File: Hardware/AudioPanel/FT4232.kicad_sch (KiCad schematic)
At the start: 37 parts, among them U30 93LCxxA, U57 AP2112K-3.3, U59 FT4232H, Y5 12MHz

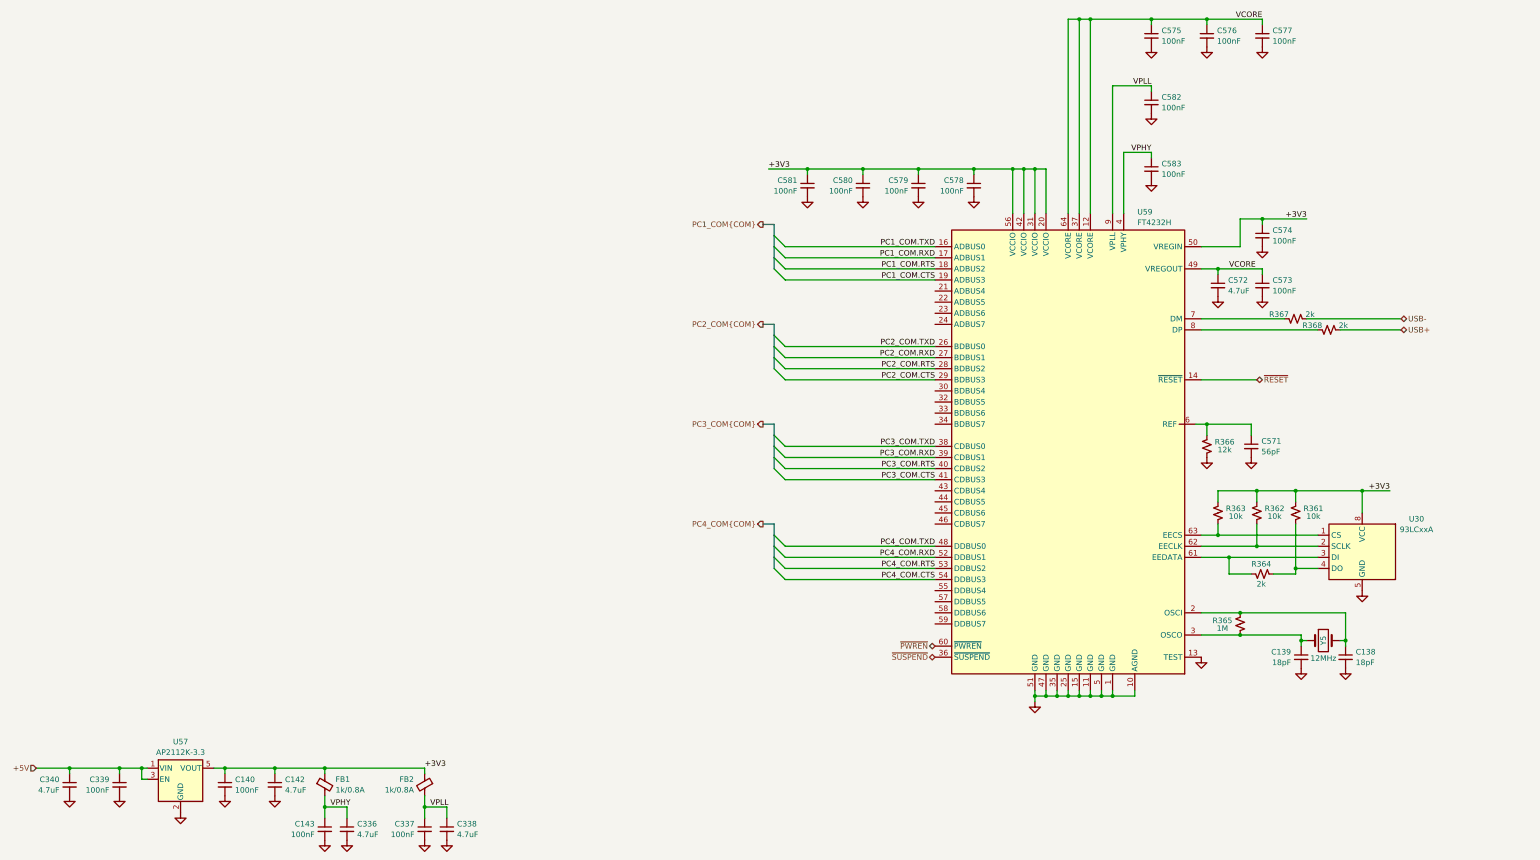
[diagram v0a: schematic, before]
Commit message: Realized that I need to rethink how I'm going to mix the radio audio with the stereo audio
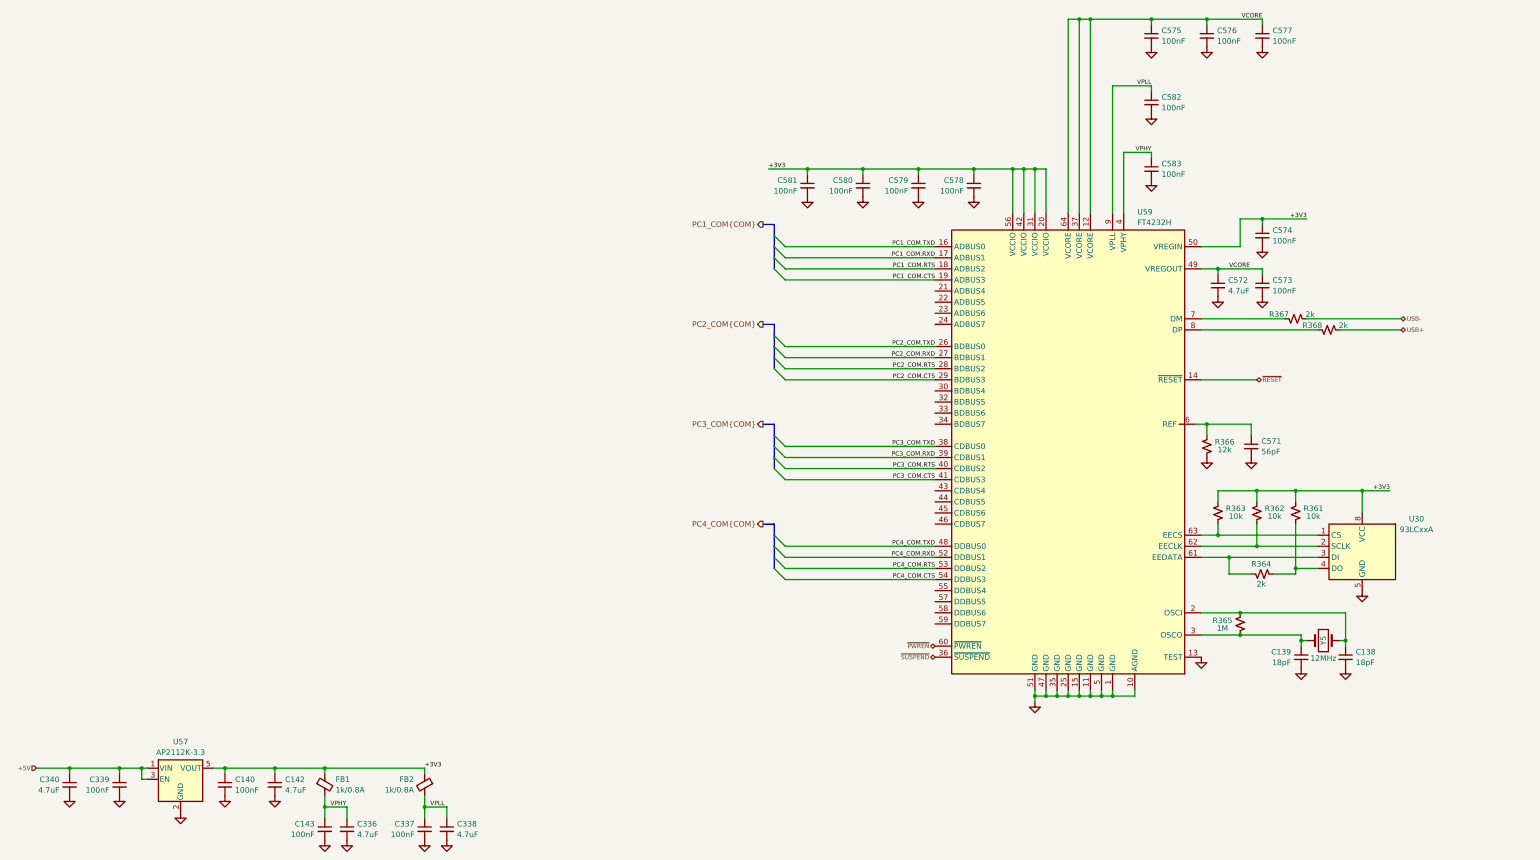
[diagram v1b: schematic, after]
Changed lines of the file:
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@@
 		(effects
 			(font
-				(size 1.27 1.27)
+				(size 1 1)
 			)
 			(justify right bottom)
@@
 		(effects
 			(font
-				(size 1.27 1.27)
+				(size 1 1)
 			)
 			(justify left bottom)
@@
 		(effects
 			(font
-				(size 1.27 1.27)
+				(size 1 1)
 			)
 			(justify right bottom)
@@
 		(effects
 			(font
-				(size 1.27 1.27)
+				(size 1 1)
 			)
 			(justify right bottom)
@@
 		(effects
 			(font
-				(size 1.27 1.27)
+				(size 1 1)
 			)
 			(justify right bottom)
@@
 		(effects
 			(font
-				(size 1.27 1.27)
+				(size 1 1)
 			)
 			(justify right bottom)
@@
 		(effects
 			(font
-				(size 1.27 1.27)
+				(size 1 1)
 			)
 			(justify right bottom)
@@
 		(effects
 			(font
-				(size 1.27 1.27)
+				(size 1 1)
 			)
 			(justify right bottom)
@@
 		(effects
 			(font
-				(size 1.27 1.27)
+				(size 1 1)
 			)
 			(justify right bottom)
@@
 		(effects
 			(font
-				(size 1.27 1.27)
+				(size 1 1)
 			)
 			(justify right bottom)
@@
 		(effects
 			(font
-				(size 1.27 1.27)
+				(size 1 1)
 			)
 			(justify right bottom)
@@
 		(effects
 			(font
-				(size 1.27 1.27)
+				(size 1 1)
 			)
 			(justify right bottom)
@@
 		(effects
 			(font
-				(size 1.27 1.27)
+				(size 1 1)
 			)
 			(justify right bottom)
@@
 		(effects
 			(font
-				(size 1.27 1.27)
+				(size 1 1)
 			)
 			(justify left bottom)
@@
 		(effects
 			(font
-				(size 1.27 1.27)
+				(size 1 1)
 			)
 			(justify right bottom)
@@
 		(effects
 			(font
-				(size 1.27 1.27)
+				(size 1 1)
 			)
 			(justify left bottom)
@@
 		(effects
 			(font
-				(size 1.27 1.27)
+				(size 1 1)
 			)
 			(justify right bottom)
@@
 		(effects
 			(font
-				(size 1.27 1.27)
+				(size 1 1)
 			)
 			(justify right bottom)
@@
 		(effects
 			(font
-				(size 1.27 1.27)
+				(size 1 1)
 			)
 			(justify right bottom)
@@
 		(effects
 			(font
-				(size 1.27 1.27)
+				(size 1 1)
 			)
 			(justify right bottom)
@@
 		(effects
 			(font
-				(size 1.27 1.27)
+				(size 1 1)
 			)
 			(justify right bottom)
@@
 		(effects
 			(font
-				(size 1.27 1.27)
+				(size 1 1)
 			)
 			(justify left bottom)
@@
 		(effects
 			(font
-				(size 1.27 1.27)
+				(size 1 1)
 			)
 			(justify right bottom)
@@
 		(effects
 			(font
-				(size 1.27 1.27)
+				(size 1 1)
 			)
 			(justify right bottom)
@@
 		(effects
 			(font
-				(size 1.27 1.27)
+				(size 1 1)
 			)
 			(justify left bottom)
@@
 		(effects
 			(font
-				(size 1.27 1.27)
+				(size 1 1)
 			)
 			(justify right bottom)
@@
 		(effects
 			(font
-				(size 1.27 1.27)
+				(size 1 1)
 			)
 			(justify right)
@@
 		(effects
 			(font
-				(size 1.27 1.27)
+				(size 1 1)
 			)
 			(justify right)
@@
 		(effects
 			(font
-				(size 1.27 1.27)
+				(size 1 1)
 			)
 			(justify left)
@@
 		(effects
 			(font
-				(size 1.27 1.27)
+				(size 1 1)
 			)
 			(justify left)
@@
 		(effects
 			(font
-				(size 1.27 1.27)
+				(size 1 1)
 			)
 			(justify left)
@@
 		(effects
 			(font
-				(size 1.27 1.27)
-			)
-			(justify right)
+				(size 1 1)
+			)
+			(justify right)

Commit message: Cleaned up stuff, defined more busses
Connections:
- net FT4232_USB-: now reaches R368.1, U59.8 (DP)
- net FT4232_USB+: now reaches R367.1, U59.7 (DM)
- net USB+ renamed FT4232H.D-
- net USB- renamed FT4232H.D+
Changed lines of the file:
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@@
+	)
+	(bus_entry
+		(at 367.03 99.06)
+		(size -2.54 2.54)
+		(stroke
+			(width 0)
+			(type default)
+		)
 	)
 	(bus_entry
@@
 	)
 	(bus_entry
+		(at 367.03 99.06)
+		(size -2.54 2.54)
+		(stroke
+			(width 0)
+			(type default)
+		)
+	)
+	(bus_entry
 		(at 210.82 158.75)
 		(size 2.54 2.54)
@@
 	)
 	(bus_entry
+		(at 367.03 101.6)
+		(size -2.54 2.54)
+		(stroke
+			(width 0)
+			(type default)
+		)
+	)
+	(bus_entry
 		(at 210.82 87.63)
 		(size 2.54 2.54)
@@
 		)
 	)
+	(bus_entry
+		(at 367.03 101.6)
+		(size -2.54 2.54)
+		(stroke
+			(width 0)
+			(type default)
+		)
+	)
 	(wire
 		(pts
@@
 	(wire
 		(pts
-			(xy 332.74 101.6) (xy 354.33 101.6)
+			(xy 332.74 101.6) (xy 364.49 101.6)
 		)
 		(stroke
@@
 		)
 	)
+	(bus
+		(pts
+			(xy 367.03 96.52) (xy 367.03 99.06)
+		)
+		(stroke
+			(width 0)
+			(type default)
+		)
+	)
 	(wire
 		(pts
@@
 		)
 	)
+	(bus
+		(pts
+			(xy 367.03 99.06) (xy 367.03 101.6)
+		)
+		(stroke
+			(width 0)
+			(type default)
+		)
+	)
 	(wire
 		(pts
@@
 	(wire
 		(pts
-			(xy 340.36 104.14) (xy 354.33 104.14)
+			(xy 340.36 104.14) (xy 364.49 104.14)
 		)
 		(stroke
@@
 		)
 	)
+	(label "FT4232H.D+"
+		(at 349.25 101.6 0)
+		(effects
+			(font
+				(size 1.27 1.27)
+			)
+			(justify left bottom)
+		)
+	)
 	(label "PC1_COM.TXD"
 		(at 247.65 85.09 180)
@@
 		)
 	)
+	(label "FT4232_USB-"
+		(at 308.61 104.14 0)
+		(effects
+			(font
+				(size 1 1)
+			)
+			(justify left bottom)
+		)
+	)
 	(label "PC4_COM.TXD"
 		(at 247.65 153.67 180)
@@
 		)
 	)
+	(label "FT4232_USB+"
+		(at 308.61 101.6 0)
+		(effects
+			(font
+				(size 1 1)
+			)
+			(justify left bottom)
+		)
+	)
 	(label "+3V3"
 		(at 130.81 204.47 0)
@@
 			)
 			(justify right bottom)
+		)
+	)
+	(label "FT4232H.D-"
+		(at 349.25 104.14 0)
+		(effects
+			(font
+				(size 1.27 1.27)
+			)
+			(justify left bottom)
 		)
 	)
@@
 		)
 	)
-	(hierarchical_label "USB-"
+	(hierarchical_label "FT4232H{USB}"
 		(shape bidirectional)
-		(at 354.33 101.6 0)
-		(effects
-			(font
-				(size 1 1)
+		(at 367.03 96.52 0)
+		(effects
+			(font
+				(size 1.27 1.27)
 			)
 			(justify left)
@@
 		)
 	)
-	(hierarchical_label "USB+"
-		(shape bidirectional)
-		(at 354.33 104.14 0)
-		(effects
-			(font
-				(size 1 1)
-			)
-			(justify left)
-		)
-	)
